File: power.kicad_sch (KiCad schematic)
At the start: 33 parts, among them IC1 TLV62569DBVR, J5 Power Out, J6 Power In 12V, U1 TPS54302

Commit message: Added ORing VBUS
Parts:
- added C60, C61: 100n, Capacitor_SMD:C_0603_1608Metric_Pad1.08x0.95mm_HandSolder, symbol Device:C_Small
- added D4: 5V_S, LED_SMD:LED_0805_2012Metric_Pad1.15x1.40mm_HandSolder, symbol Device:LED
- added IC2: TPS2113APW, SamacSys_Parts:NE555DR, symbol SamacSys_Parts:TPS2113APW
- added R10: 36k, Resistor_SMD:R_0805_2012Metric_Pad1.20x1.40mm_HandSolder, symbol Device:R_Small
- added R11: 500, Resistor_SMD:R_0603_1608Metric_Pad0.98x0.95mm_HandSolder, symbol Device:R_Small
- added R12: 10k, Resistor_SMD:R_0805_2012Metric_Pad1.20x1.40mm_HandSolder, symbol Device:R_Small
- added R31: 2k2, Resistor_SMD:R_0805_2012Metric_Pad1.20x1.40mm_HandSolder, symbol Device:R_Small
- added R9: 157k, Resistor_SMD:R_0805_2012Metric_Pad1.20x1.40mm_HandSolder, symbol Device:R_Small
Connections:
- net +5V Buck: now also C60.1, IC2.8 (IN1), R9.1; no longer C7.2, C9.1, IC1.1 (EN), IC1.4 (VIN), J5.2 (Pin_2), R29.1
- net GND: now also C60.2, C61.2, IC2.2 (~{EN}), IC2.5 (GND), R10.2, R11.2, R31.2
- new net: D4.1 (K), R31.1
- new net: D4.2 (A), IC2.1 (STAT), R12.1
- new net: IC2.4 (ILIM), R11.1
- new net: IC2.3 (VSNS), R10.1, R9.2
- new net +5V: C7.2, C9.1, IC1.1 (EN), IC1.4 (VIN), IC2.7 (OUT), J5.2 (Pin_2), R12.2, R29.1
- new net VBUS: C61.1, IC2.6 (IN2)
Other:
- note added: "0.8=4.3 * R2 / (R2 + R1) => R2 = 36k; R1 = 157k"
- note added: "I_lim = 500 / R_lim => R_lim = 500 Ohm (I_lim = 1A)"
- note added: "If +5V Buck falls below 4.3V (or OFF), switch to VBUS"
- note added: "LED ON = +5V Buck LED OFF = VBUS"

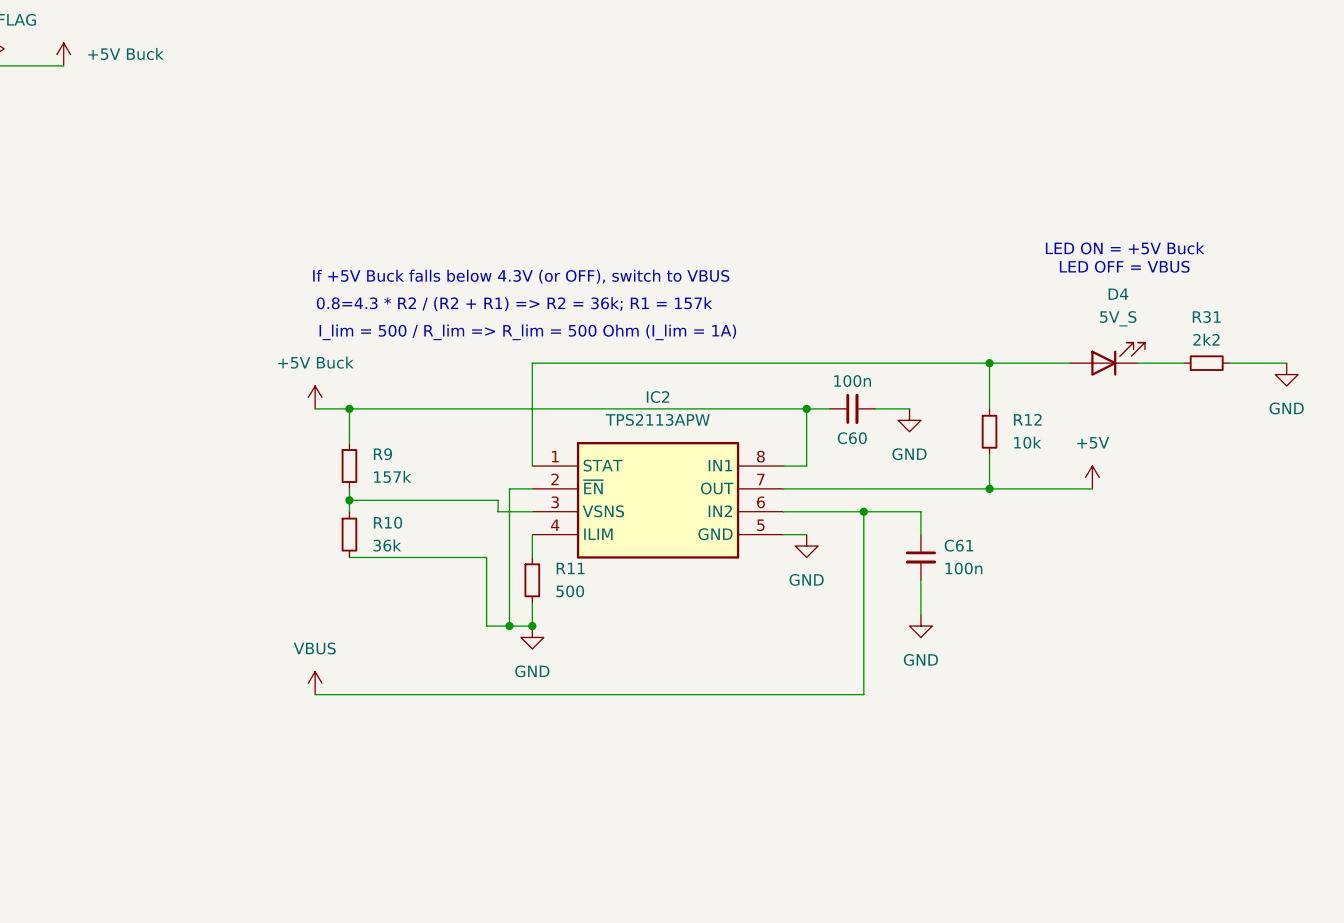
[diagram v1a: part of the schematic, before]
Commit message: Added LED indicators, USER LEDs, extended layout, fixed footprints
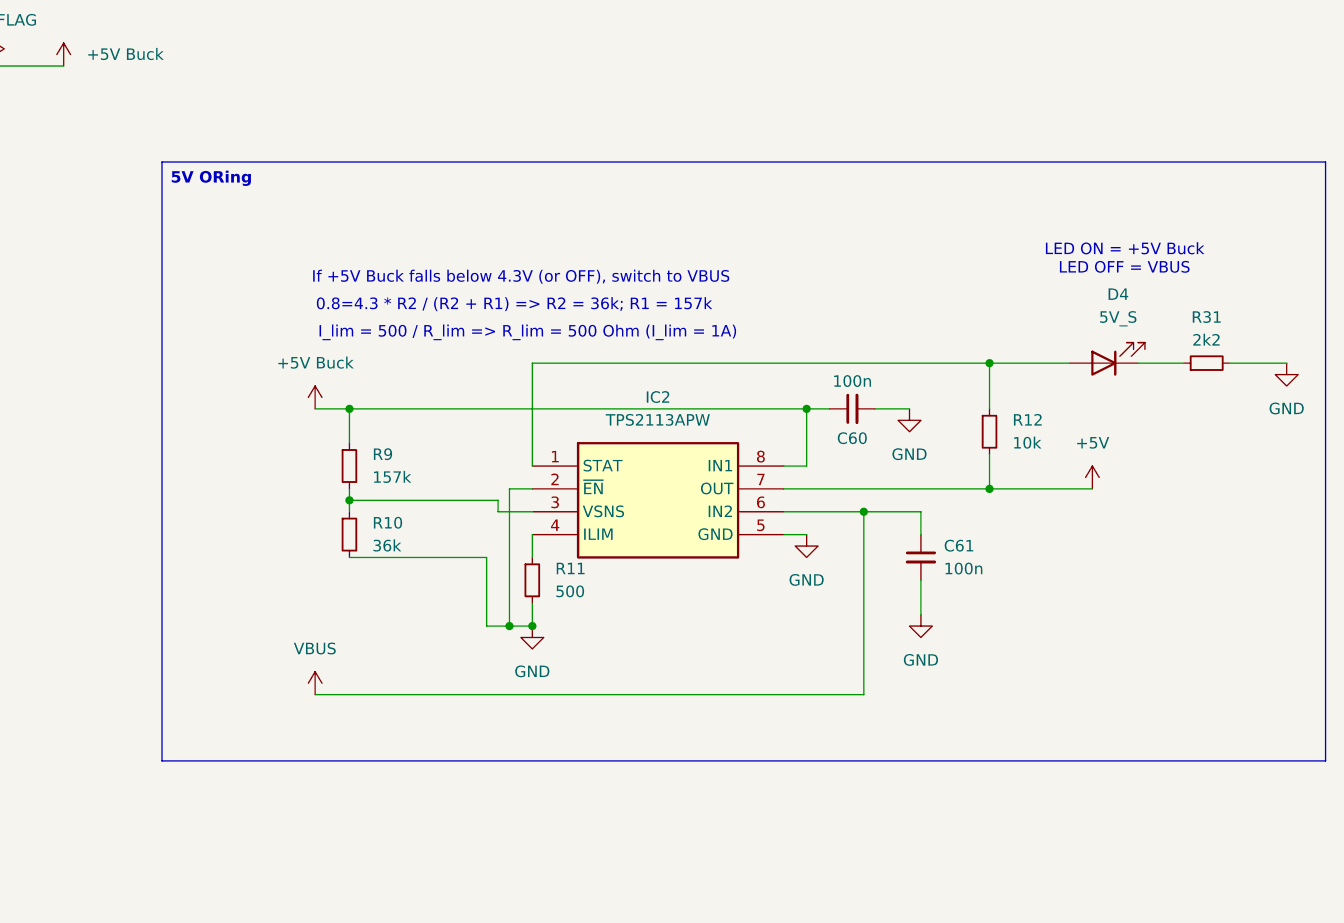
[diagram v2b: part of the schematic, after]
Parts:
- D10, D11, D12: footprint LED_SMD:LED_0603_1608Metric_Pad1.05x0.95mm_HandSolder -> LED_SMD:LED_0805_2012Metric_Pad1.15x1.40mm_HandSolder
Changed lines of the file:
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@@
 		)
 	)
+	(text_box "5V ORing"
+		(exclude_from_sim no)
+		(at 271.272 60.198 0)
+		(size 129.286 66.548)
+		(margins 0.9525 0.9525 0.9525 0.9525)
+		(stroke
+			(width 0)
+			(type solid)
+		)
+		(fill
+			(type none)
+		)
+		(effects
+			(font
+				(size 1.27 1.27)
+				(thickness 0.254)
+				(bold yes)
+			)
+			(justify left top)
+		)
+	)
 	(junction
 		(at 252.73 49.53)
@@
 			)
 		)
-		(property "Footprint" "LED_SMD:LED_0603_1608Metric_Pad1.05x0.95mm_HandSolder"
+		(property "Footprint" "LED_SMD:LED_0805_2012Metric_Pad1.15x1.40mm_HandSolder"
 			(at 44.45 172.72 0)
 			(effects
@@
 			)
 		)
-		(property "Footprint" "LED_SMD:LED_0603_1608Metric_Pad1.05x0.95mm_HandSolder"
+		(property "Footprint" "LED_SMD:LED_0805_2012Metric_Pad1.15x1.40mm_HandSolder"
 			(at 44.45 189.23 0)
 			(effects
@@
 			)
 		)
-		(property "Footprint" "LED_SMD:LED_0603_1608Metric_Pad1.05x0.95mm_HandSolder"
+		(property "Footprint" "LED_SMD:LED_0805_2012Metric_Pad1.15x1.40mm_HandSolder"
 			(at 44.45 156.21 0)
 			(effects

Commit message: Added changes
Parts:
- C12: footprint Capacitor_SMD:C_0603_1608Metric_Pad1.08x0.95mm_HandSolder -> Capacitor_SMD:C_0805_2012Metric_Pad1.18x1.45mm_HandSolder
- R11: value 500 -> 167
- R5: footprint Resistor_SMD:R_0603_1608Metric_Pad0.98x0.95mm_HandSolder -> Resistor_SMD:R_0805_2012Metric_Pad1.20x1.40mm_HandSolder
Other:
- note added: "I_lim = 500 / R_lim => R_lim = 167 Ohm (I_lim = ~3A)"
- note removed: "I_lim = 500 / R_lim => R_lim = 500 Ohm (I_lim = 1A)"
- moved on the sheet: C12, C13, C14, C15, C18, C19, C20, C21, C6, C60, C61, C7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

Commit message: Fixed USB VSENSE, fixed things
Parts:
- removed J6: Power In 12V, Connector_PinSocket_2.54mm:PinSocket_1x02_P2.54mm_Vertical, symbol Connector:Conn_01x02_Socket
- added J4: 53048-0210, SamacSys_Parts:SHDRRA2W35P0X125_1X2_425X550X350P, symbol SamacSys_Parts:53048-0210
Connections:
- net +12V In: now also J4.1
- net GND: now also J4.2
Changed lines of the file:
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@@
+	)
+	(symbol
+		(lib_id "SamacSys_Parts:53048-0210")
+		(at 266.7 224.79 0)
+		(unit 1)
+		(exclude_from_sim no)
+		(in_bom yes)
+		(on_board yes)
+		(dnp no)
+		(property "Reference" "J4"
+			(at 283.21 224.7899 0)
+			(effects
+				(font
+					(size 1.27 1.27)
+				)
+				(justify left)
+			)
+		)
+		(property "Value" "53048-0210"
+			(at 283.21 227.3299 0)
+			(effects
+				(font
+					(size 1.27 1.27)
+				)
+				(justify left)
+			)
+		)
+		(property "Footprint" "SamacSys_Parts:SHDRRA2W35P0X125_1X2_425X550X350P"
+			(at 283.21 319.71 0)
+			(effects
+				(font
+					(size 1.27 1.27)
+				)
+				(justify left top)
+				(hide yes)
+			)
+		)
+		(property "Datasheet" "https://www.molex.com/pdm_docs/sd/530481010_sd.pdf"
+			(at 283.21 419.71 0)
+			(effects
+				(font
+					(size 1.27 1.27)
+				)
+				(justify left top)
+				(hide yes)
+			)
+		)
+		(property "Description" "2 way through board PCB 90deg header Molex PICOBLADE Series, Series Number 53048, 1.25mm Pitch 2 Way 1 Row Right Angle PCB Header, Solder Termination, 1A"
+			(at 266.7 224.79 0)
+			(effects
+				(font
+					(size 1.27 1.27)
+				)
+				(hide yes)
+			)
+		)
+		(property "Height" "3.5"
+			(at 283.21 619.71 0)
+			(effects
+				(font
+					(size 1.27 1.27)
+				)
+				(justify left top)
+				(hide yes)
+			)
+		)
+		(property "Mouser Part Number" "538-53048-0210"
+			(at 283.21 719.71 0)
+			(effects
+				(font
+					(size 1.27 1.27)
+				)
+				(justify left top)
+				(hide yes)
+			)
+		)
+		(property "Mouser Price/Stock" "https://www.mouser.co.uk/ProductDetail/Molex/53048-0210?qs=o4r9IV%252BgZWMoVY43HmKPkg%3D%3D"
+			(at 283.21 819.71 0)
+			(effects
+				(font
+					(size 1.27 1.27)
+				)
+				(justify left top)
+				(hide yes)
+			)
+		)
+		(property "Manufacturer_Name" "Molex"
+			(at 283.21 919.71 0)
+			(effects
+				(font
+					(size 1.27 1.27)
+				)
+				(justify left top)
+				(hide yes)
+			)
+		)
+		(property "Manufacturer_Part_Number" "53048-0210"
+			(at 283.21 1019.71 0)
+			(effects
+				(font
+					(size 1.27 1.27)
+				)
+				(justify left top)
+				(hide yes)
+			)
+		)
+		(pin "1"
+		)
+		(pin "2"
+		)
+		(instances
+			(project "telemetry-rusolar-rework"
+				(path "/32c2c747-0685-4927-b759-a1d2bc91875e/b549e9a9-8b38-4eb3-901d-8861fcc01a4a"
+					(reference "J4")
+					(unit 1)
+				)
+			)
+		)
 	)
 	(symbol
@@
 					(unit 1)
 				)
-			)
-		)
-	)
-	(symbol
-		(lib_id "Connector:Conn_01x02_Socket")
-		(at 271.78 224.79 0)
-		(unit 1)
-		(exclude_from_sim no)
-		(in_bom yes)
-		(on_board yes)
-		(dnp no)
-		(fields_autoplaced yes)
-		(property "Reference" "J6"
-			(at 273.05 224.7899 0)
-			(effects
-				(font
-					(size 1.27 1.27)
-				)
-				(justify left)
-			)
-		)
-		(property "Value" "Power In 12V"
-			(at 273.05 227.3299 0)
-			(effects
-				(font
-					(size 1.27 1.27)
-				)
-				(justify left)
-			)
-		)
-		(property "Footprint" "Connector_PinSocket_2.54mm:PinSocket_1x02_P2.54mm_Vertical"
-			(at 271.78 224.79 0)
-			(effects
-				(font
-					(size 1.27 1.27)
-				)
-				(hide yes)
-			)
-		)
-		(property "Datasheet" "~"
-			(at 271.78 224.79 0)
-			(effects
-				(font
-					(size 1.27 1.27)
-				)
-				(hide yes)
-			)
-		)
-		(property "Description" "Generic connector, single row, 01x02, script generated"
-			(at 271.78 224.79 0)
-			(effects
-				(font
-					(size 1.27 1.27)
-				)
-				(hide yes)
-			)
-		)
-		(pin "1"
-		)
-		(pin "2"
-		)
-		(instances
-			(project ""
-				(path "/32c2c747-0685-4927-b759-a1d2bc91875e/b549e9a9-8b38-4eb3-901d-8861fcc01a4a"
-					(reference "J6")
-					(unit 1)
-				)

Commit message: Fixed things
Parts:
- removed C60, C61: 100n, Capacitor_SMD:C_0603_1608Metric_Pad1.08x0.95mm_HandSolder, symbol Device:C_Small
- removed D4: 5V_S, LED_SMD:LED_0805_2012Metric_Pad1.15x1.40mm_HandSolder, symbol Device:LED
- removed IC2: TPS2113APW, SamacSys_Parts:NE555DR, symbol SamacSys_Parts:TPS2113APW
- removed R10: 36k, Resistor_SMD:R_0805_2012Metric_Pad1.20x1.40mm_HandSolder, symbol Device:R_Small
- removed R11: 167, Resistor_SMD:R_0603_1608Metric_Pad0.98x0.95mm_HandSolder, symbol Device:R_Small
- removed R12: 10k, Resistor_SMD:R_0805_2012Metric_Pad1.20x1.40mm_HandSolder, symbol Device:R_Small
- removed R31: 2k2, Resistor_SMD:R_0805_2012Metric_Pad1.20x1.40mm_HandSolder, symbol Device:R_Small
- removed R9: 157k, Resistor_SMD:R_0805_2012Metric_Pad1.20x1.40mm_HandSolder, symbol Device:R_Small
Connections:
- net +5V is gone; now on net +5V Buck: C7.2, C9.1, IC1.1 (EN), IC1.4 (VIN), J5.2 (Pin_2), R29.1
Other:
- note removed: "0.8=4.3 * R2 / (R2 + R1) => R2 = 36k; R1 = 157k"
- note removed: "I_lim = 500 / R_lim => R_lim = 167 Ohm (I_lim = ~3A)"
- note removed: "If +5V Buck falls below 4.3V (or OFF), switch to VBUS"
- note removed: "LED ON = +5V Buck LED OFF = VBUS"
